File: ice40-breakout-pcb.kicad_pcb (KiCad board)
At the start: 2 copper layers, 56 x 71.8 mm, 63 parts, among them J1 USB_B_Micro, J2 USB_Break_Out, J3 Conn_02x16_Odd_Even, J4 Conn_02x16_Odd_Even, J5 Conn_02x16_Odd_Even, J6 Conn_02x04_Odd_Even, U1 SIT2001BI-S2-33E-12.000000G, U2 TLV73333PDBV, U3 TLV73312PDBV, U4 AT25SF081-SHD-X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

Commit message: Fix-up USB routing.
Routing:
- net Net-(J1-Pad2): track 0.00 -> 12.3 mm
- net Net-(J1-Pad3): track 4.40 -> 13.8 mm
- net Net-(J1-Pad4): track 0.00 -> 5.31 mm
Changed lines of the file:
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@@
     (thickness 1.6)
     (drawings 8)
-    (tracks 755)
+    (tracks 767)
     (zones 0)
     (modules 63)
@@
   (segment (start 126.0125 127.9375) (end 126.85 127.1) (width 0.3) (layer F.Cu) (net 11) (status 20))
   (segment (start 122.9 127.9375) (end 126.0125 127.9375) (width 0.3) (layer F.Cu) (net 11) (status 10))
-  (segment (start 120 116.1) (end 118.4 114.5) (width 0.18) (layer F.Cu) (net 14) (status 20))
-  (segment (start 121.3 114.8) (end 120 116.1) (width 0.18) (layer F.Cu) (net 14) (status 10))
   (segment (start 121.3 114.5) (end 121.3 114.8) (width 0.18) (layer F.Cu) (net 14) (status 30))
   (segment (start 117.465031 108.665031) (end 121.3 112.5) (width 0.18) (layer F.Cu) (net 15) (status 20))
@@
   (segment (start 114.16502 113.05998) (end 114.16502 105.59748) (width 0.3) (layer F.Cu) (net 3))
   (segment (start 110.725 116.5) (end 114.16502 113.05998) (width 0.3) (layer F.Cu) (net 3))
+  (segment (start 117.43 116.43) (end 115.5 114.5) (width 0.18) (layer F.Cu) (net 12))
+  (segment (start 117.43 120.7) (end 117.43 116.43) (width 0.18) (layer F.Cu) (net 12))
+  (segment (start 119.35 122.62) (end 117.43 120.7) (width 0.18) (layer F.Cu) (net 12))
+  (segment (start 119.35 125.2375) (end 119.35 122.62) (width 0.18) (layer F.Cu) (net 12))
+  (segment (start 120.77999 122.43001) (end 122.51 120.7) (width 0.18) (layer F.Cu) (net 13))
+  (segment (start 120.65 124.95) (end 120.77999 124.82001) (width 0.18) (layer F.Cu) (net 13))
+  (segment (start 120.77999 124.82001) (end 120.77999 122.43001) (width 0.18) (layer F.Cu) (net 13))
+  (segment (start 120.65 125.2375) (end 120.65 124.95) (width 0.18) (layer F.Cu) (net 13))
+  (segment (start 119.97 116.07) (end 118.4 114.5) (width 0.18) (layer F.Cu) (net 14))
+  (segment (start 119.97 120.7) (end 119.97 116.07) (width 0.18) (layer F.Cu) (net 14))
+  (segment (start 121.3 114.74) (end 119.97 116.07) (width 0.18) (layer F.Cu) (net 14))
+  (segment (start 121.3 114.5) (end 121.3 114.74) (width 0.18) (layer F.Cu) (net 14))
+  (segment (start 120 120.73) (end 119.97 120.7) (width 0.18) (layer F.Cu) (net 14))
+  (segment (start 120 125.2375) (end 120 120.73) (width 0.18) (layer F.Cu) (net 14))
   (segment (start 108.675 119.375) (end 108.7 119.4) (width 0.18) (layer F.Cu) (net 28))
   (segment (start 108.675 116.5) (end 108.675 119.375) (width 0.18) (layer F.Cu) (net 28))

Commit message: Add missing 3v3 route.
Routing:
- net +3V3: track 354.0 -> 358.3 mm
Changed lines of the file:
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@@
     (thickness 1.6)
     (drawings 8)
-    (tracks 767)
+    (tracks 770)
     (zones 0)
     (modules 63)
@@
   )
   (setup
-    (last_trace_width 0.18)
+    (last_trace_width 0.3)
     (user_trace_width 0.3)
     (trace_clearance 0.18)
@@
   (segment (start 113.628402 96.75) (end 115.75 94.628402) (width 0.5) (layer F.Cu) (net 3))
   (segment (start 112.521598 96.75) (end 113.628402 96.75) (width 0.5) (layer F.Cu) (net 3))
-  (segment (start 113.628402 96.75) (end 117.65 96.75) (width 0.5) (layer F.Cu) (net 3))
   (segment (start 117.7 96.75) (end 123.68001 90.76999) (width 0.5) (layer F.Cu) (net 3))
   (segment (start 117.65 96.75) (end 117.7 96.75) (width 0.5) (layer F.Cu) (net 3))
@@
   (segment (start 114.16502 113.05998) (end 114.16502 105.59748) (width 0.3) (layer F.Cu) (net 3))
   (segment (start 110.725 116.5) (end 114.16502 113.05998) (width 0.3) (layer F.Cu) (net 3))
+  (segment (start 115.75 97.8) (end 114.7 96.75) (width 0.3) (layer F.Cu) (net 3))
+  (segment (start 115.75 100.6625) (end 115.75 97.8) (width 0.3) (layer F.Cu) (net 3))
+  (segment (start 114.7 96.75) (end 117.65 96.75) (width 0.5) (layer F.Cu) (net 3))
+  (segment (start 113.628402 96.75) (end 114.7 96.75) (width 0.5) (layer F.Cu) (net 3))
   (segment (start 117.43 116.43) (end 115.5 114.5) (width 0.18) (layer F.Cu) (net 12))
   (segment (start 117.43 120.7) (end 117.43 116.43) (width 0.18) (layer F.Cu) (net 12))

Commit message: Use wider trace for 3v3 power to external connector & add GND plane.
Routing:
- net +3V3: track 358.3 -> 387.0 mm
- added copper zone on B.Cu, net GND

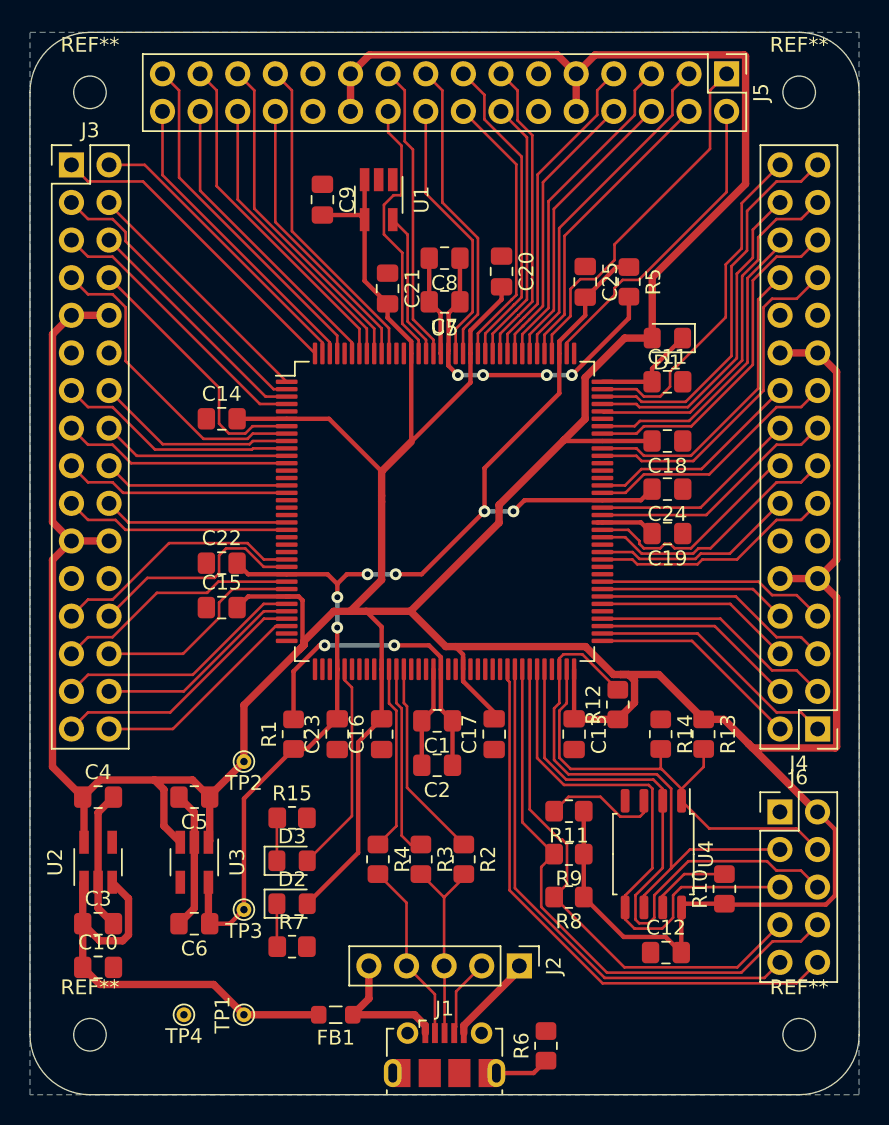
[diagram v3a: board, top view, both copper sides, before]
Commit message: Add ground vias.
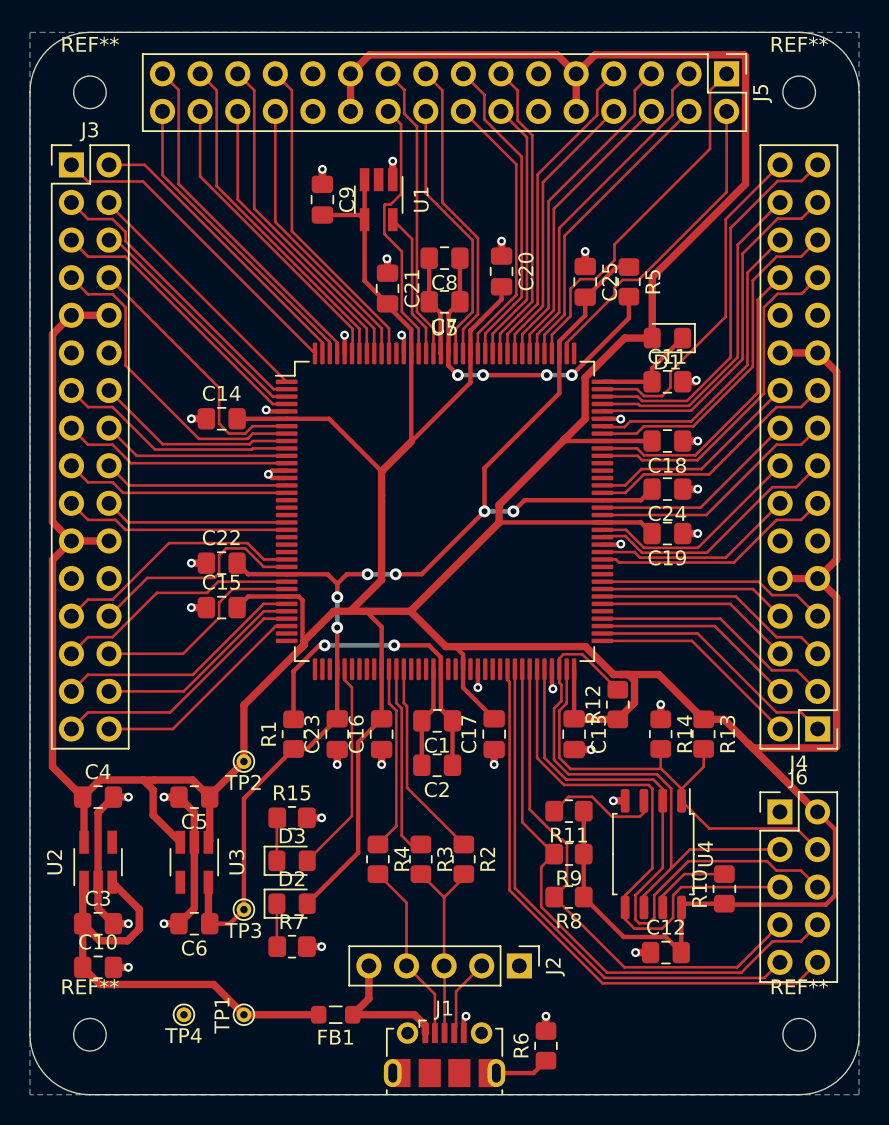
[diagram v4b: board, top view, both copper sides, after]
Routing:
- net GND: track 24.9 -> 59.1 mm, vias 0 -> 36
- net +3V3: track 387.0 -> 394.4 mm
- net +5V: track 30.9 -> 31.7 mm
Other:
- net class Default: clearance 0.18 -> 0.15
- net class Power: clearance 0.18 -> 0.15
- net class Power (Wider): clearance 0.18 -> 0.15
- rule trace_clearance: 0.18 -> 0.15

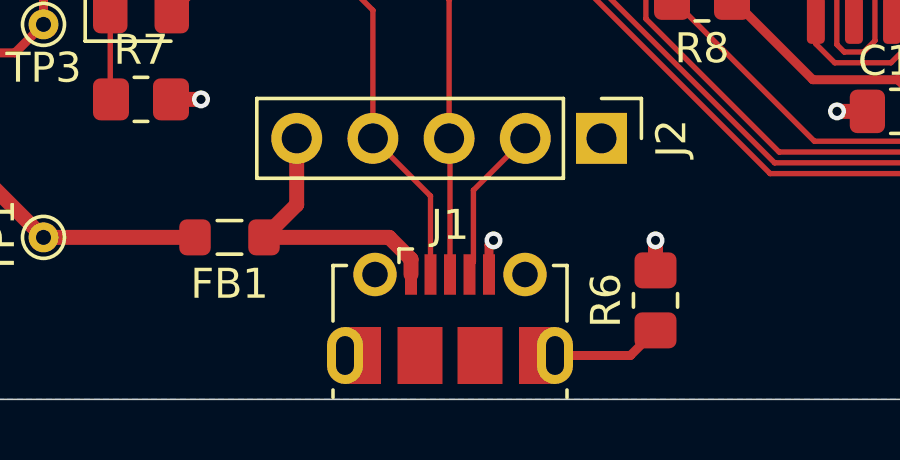
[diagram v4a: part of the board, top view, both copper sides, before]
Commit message: Connect USB socket pads to keep DRC happy.
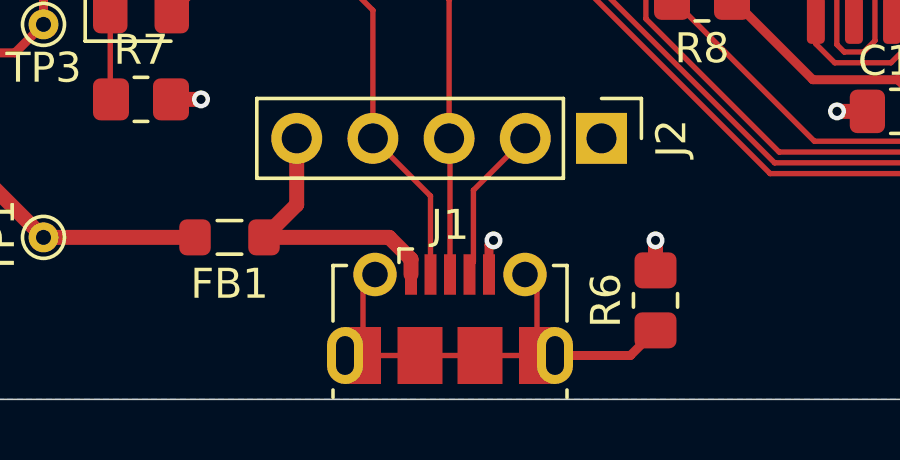
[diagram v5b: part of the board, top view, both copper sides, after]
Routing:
- net Net-(J1-Pad6): track 4.30 -> 15.8 mm

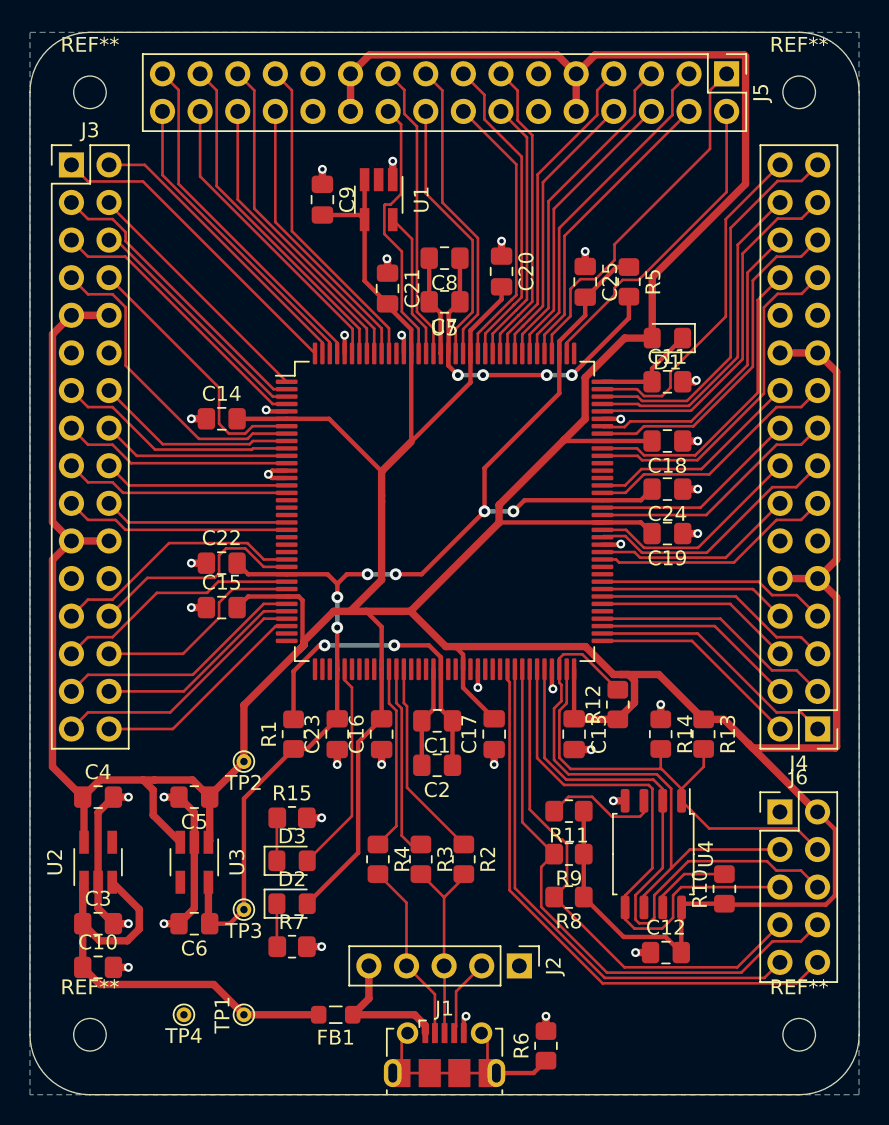
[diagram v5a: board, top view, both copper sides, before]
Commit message: Fix-up front silk screen.
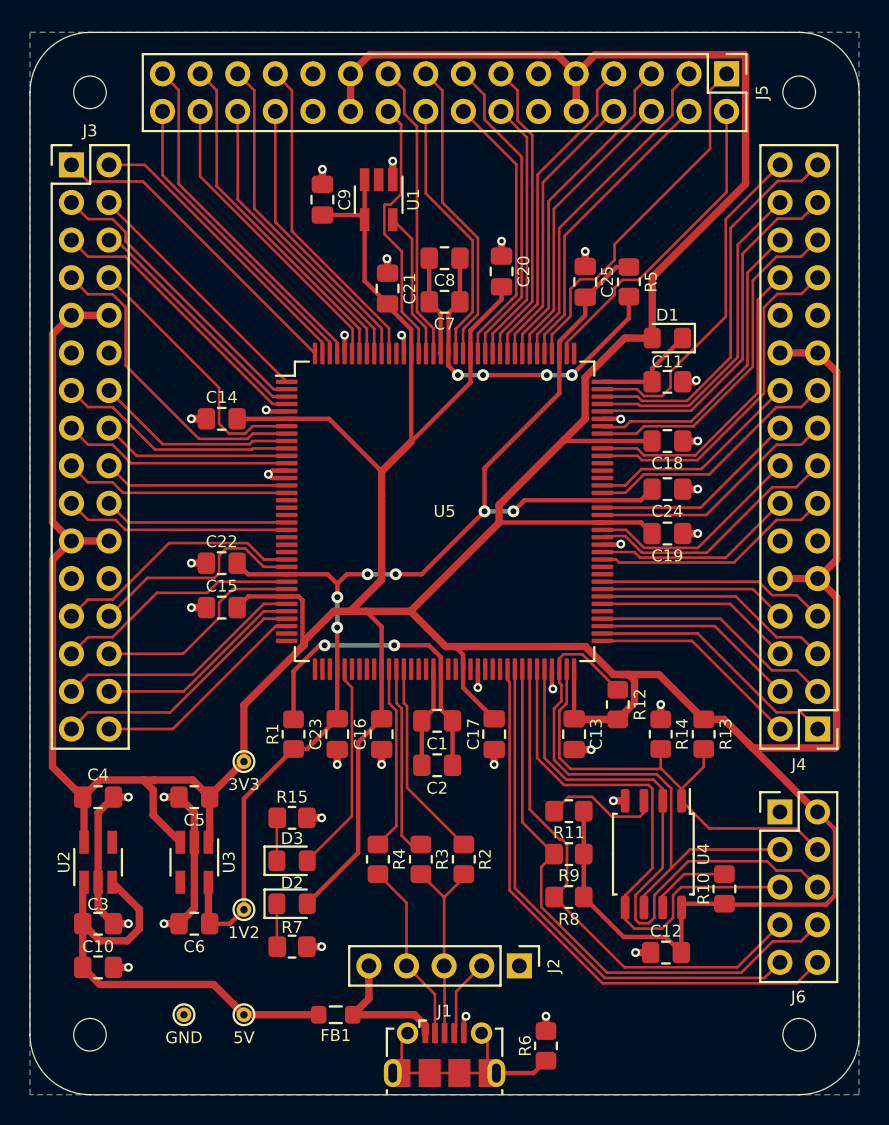
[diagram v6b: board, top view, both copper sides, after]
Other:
- board text added: "1V2"
- board text added: "3V3"
- board text added: "5V"
- board text added: "GND"

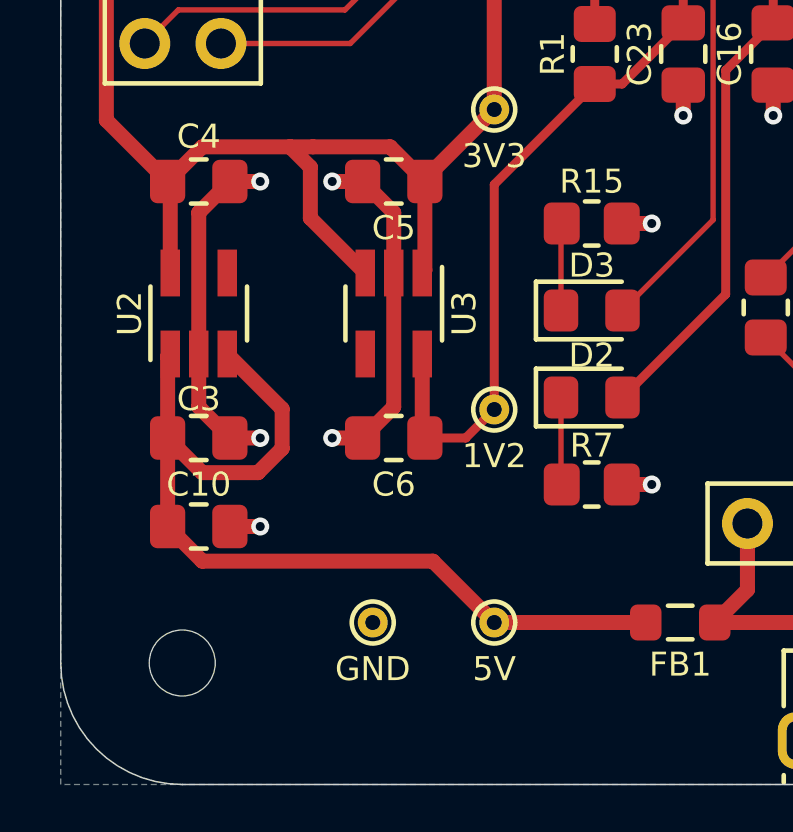
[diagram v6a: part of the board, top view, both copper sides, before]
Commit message: Fix component spacing inline with rest of layout.
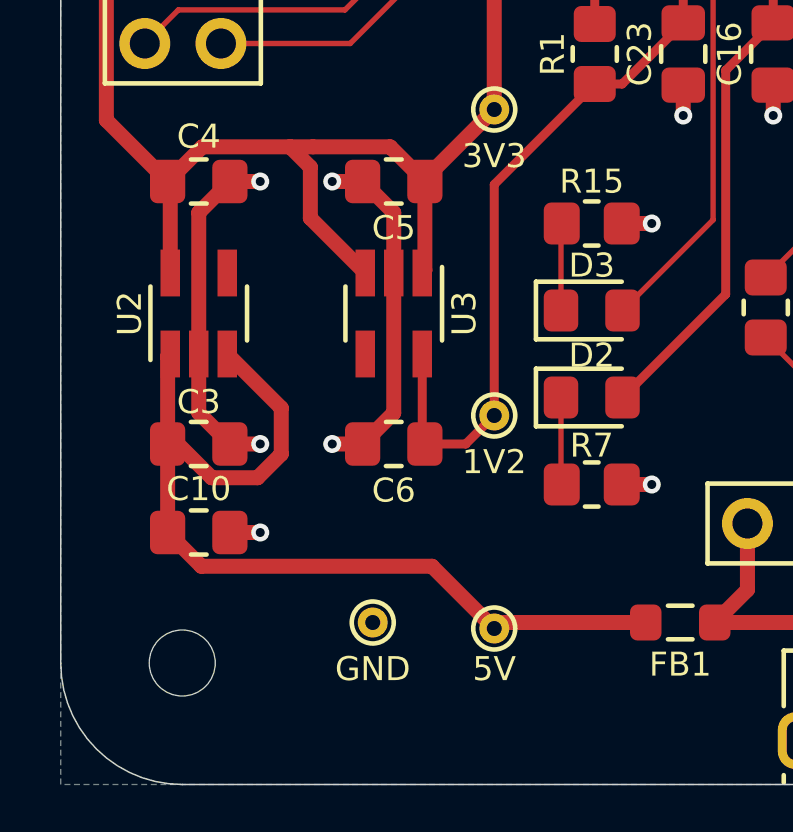
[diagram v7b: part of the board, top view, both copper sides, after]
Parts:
- moved C10 0.20 mm to (96.6, 121.0)
- moved C3 0.20 mm to (96.6, 118.0)
- moved C6 0.20 mm to (103.1, 118.0)
- moved TP1 0.20 mm to (106.5, 124.2)
- moved TP3 0.20 mm to (106.5, 117.1)
